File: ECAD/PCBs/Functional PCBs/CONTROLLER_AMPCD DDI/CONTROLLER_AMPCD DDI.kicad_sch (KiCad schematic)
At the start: 27 parts

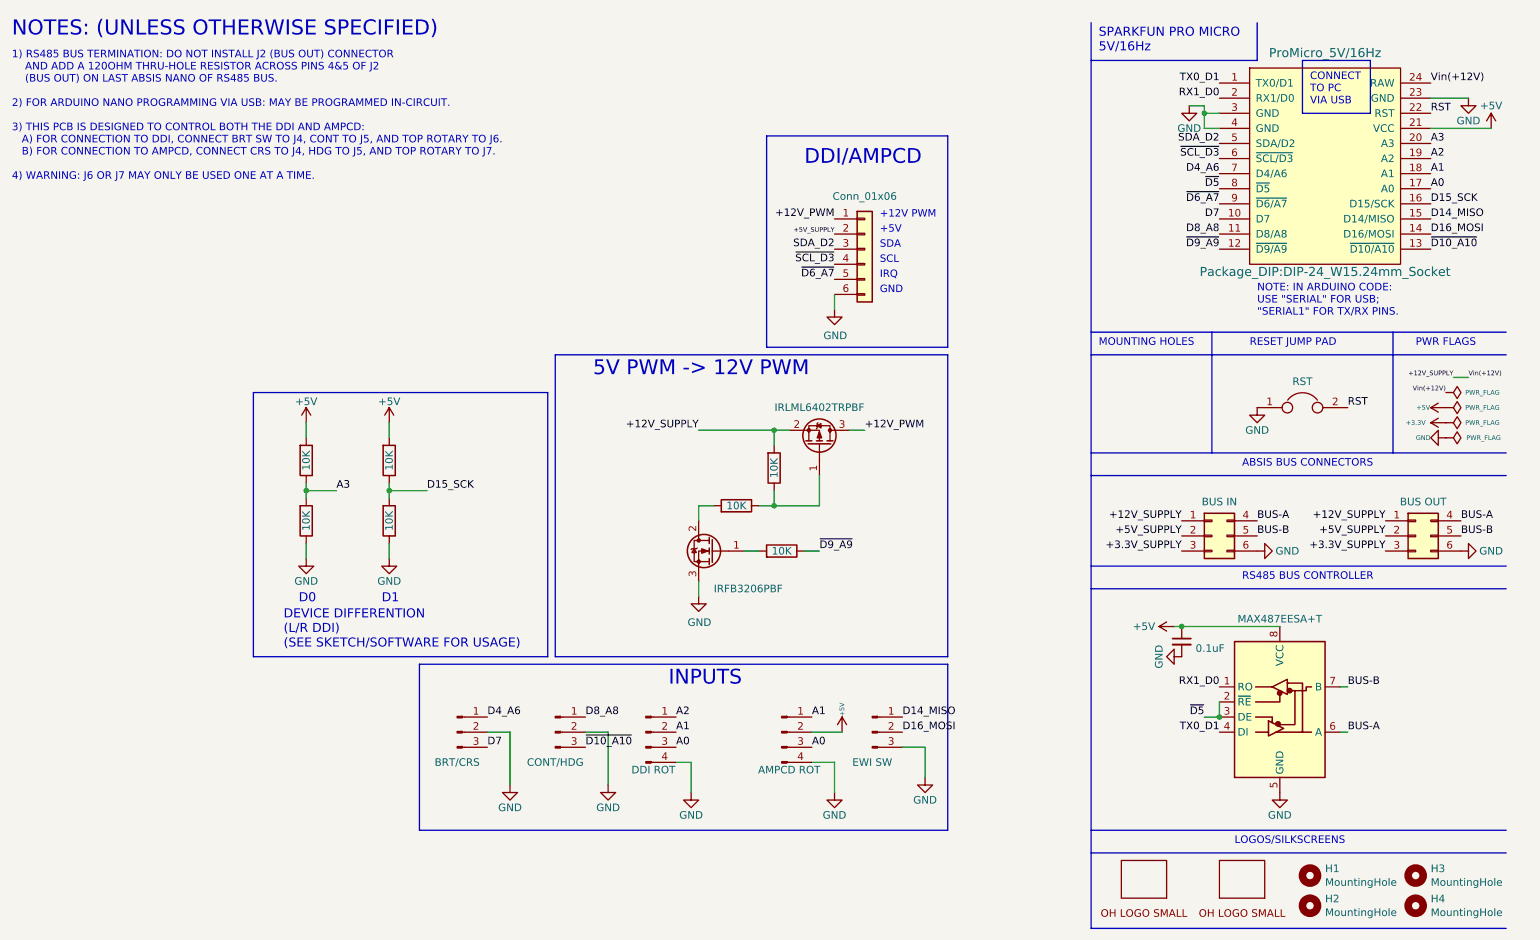
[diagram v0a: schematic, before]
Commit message: Updated DDI/AMPCD Controller
Added diode D1 between 12V and RAW pin for polarity protection.
Updated to Rev 4.
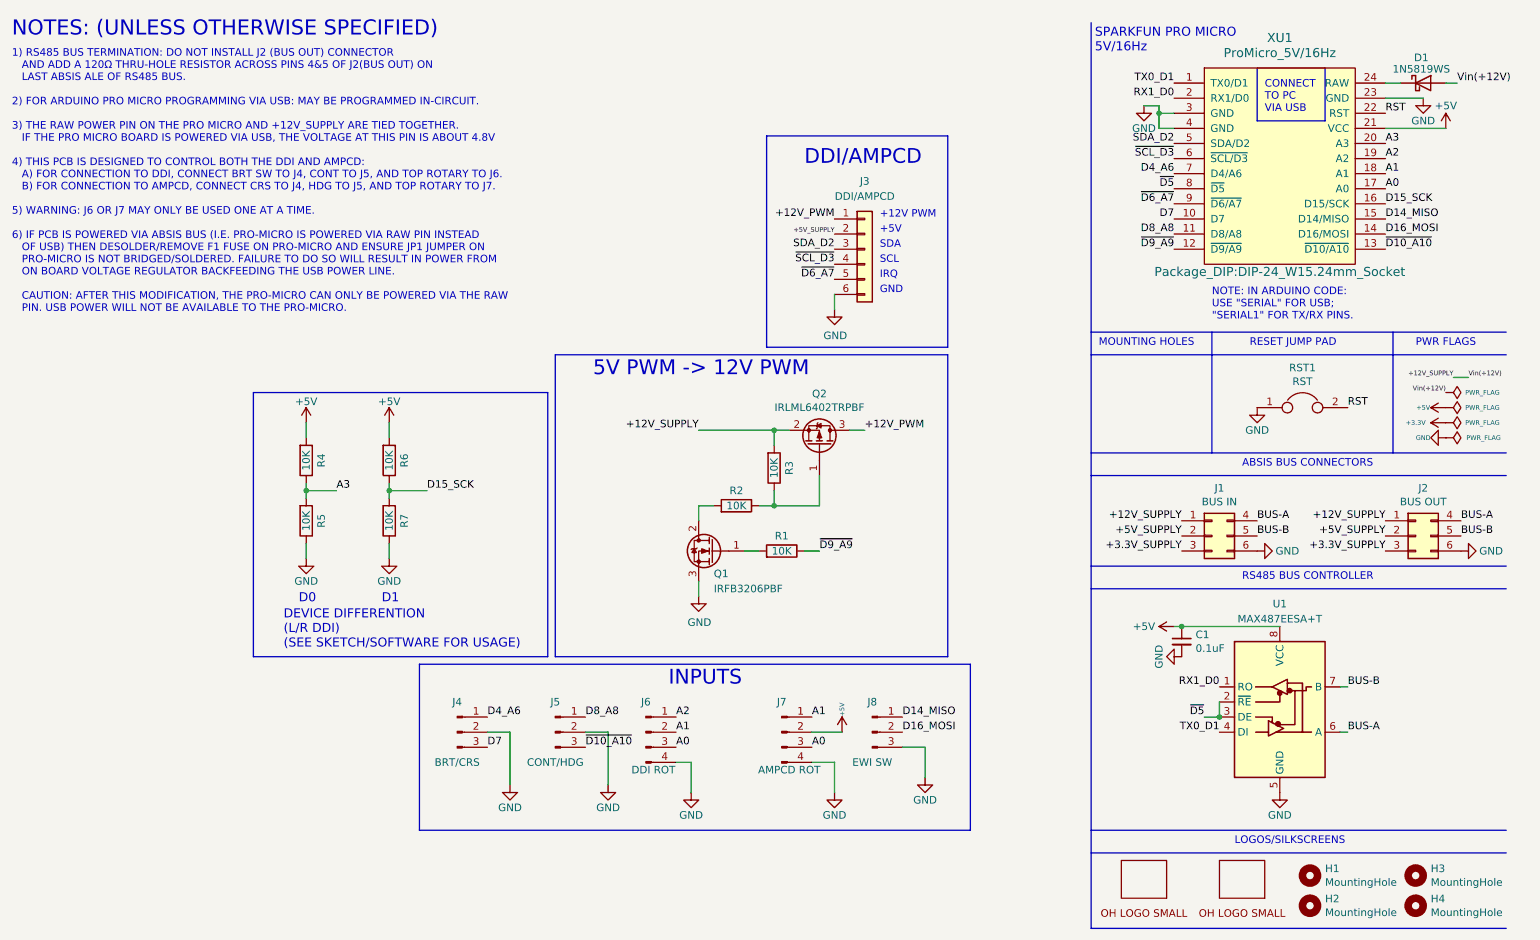
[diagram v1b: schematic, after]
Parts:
- added D1: 1N5819WS, Diode_SMD:D_SOD-323_HandSoldering, symbol Device:D_Schottky
- J3: renamed from ?; value Conn_01x06 -> DDI/AMPCD
- gave numbers to parts that had none: 20
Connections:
- net +12V_SUPPLY: now also D1.2 (A); no longer XU1.24 (RAW)
- new net: D1.1 (K), XU1.24 (RAW)
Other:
- note added: "1) RS485 BUS TERMINATION: DO NOT INSTALL J2 (BUS OUT) CONNECTOR AND ADD A 120Ω THRU-HOLE RESISTOR ACROSS PINS 4&5 OF J2(BUS OUT) ON LAST ABSIS ALE OF RS485 BUS. 2) FOR ARDUINO PRO MICRO PROGRAMMING VIA USB: MAY BE PROGRAMMED IN-CIRCUIT. 3) THE RAW POWER PIN ON THE PRO MICRO AND +12V_SUPPLY ARE TIED TOGETHER. IF THE PRO MICRO BOARD IS POWERED VIA USB, THE VOLTAGE AT THIS PIN IS ABOUT 4.8V 4) THIS 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"
- note removed: "1) RS485 BUS TERMINATION: DO NOT INSTALL J2 (BUS OUT) CONNECTOR AND ADD A 120OHM THRU-HOLE RESISTOR ACROSS PINS 4&5 OF J2 (BUS OUT) ON LAST ABSIS NANO OF RS485 BUS. 2) FOR ARDUINO NANO PROGRAMMING VIA USB: MAY BE PROGRAMMED IN-CIRCUIT. 3) THIS PCB IS DESIGNED TO CONTROL BOTH THE DDI AND AMPCD: A) FOR CONNECTION TO DDI, CONNECT BRT SW TO J4, CONT TO J5, AND TOP ROTARY TO J6. B) FOR CONNECTION TO A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"
